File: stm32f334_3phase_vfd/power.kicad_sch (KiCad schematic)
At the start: 49 parts, among them J201 Conn_02x01, J202 Conn_02x01, J205 Conn_02x01, J206 TP_VBU, J207 TP_VBV, J208 TP_VBW, J209 Conn_02x01, J212 Conn_02x01, J213 TP_TSO, J214 Conn_02x01, J215 Conn_02x01, J218 TP_CSENSE, U201 STGIB15CH60TS-L

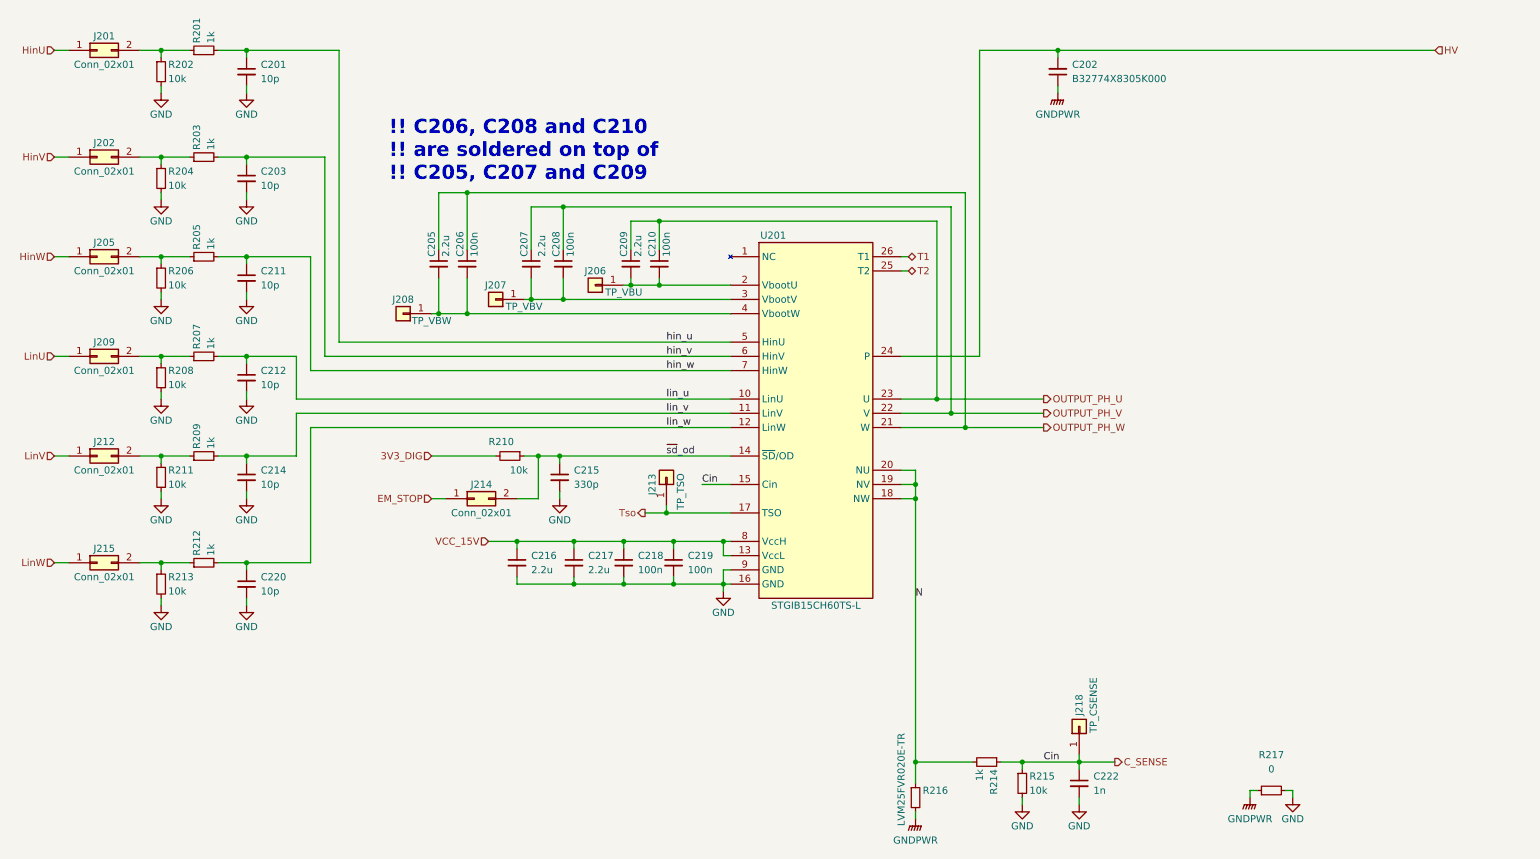
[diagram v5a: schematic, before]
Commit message: pcb fix and schematic clean-up
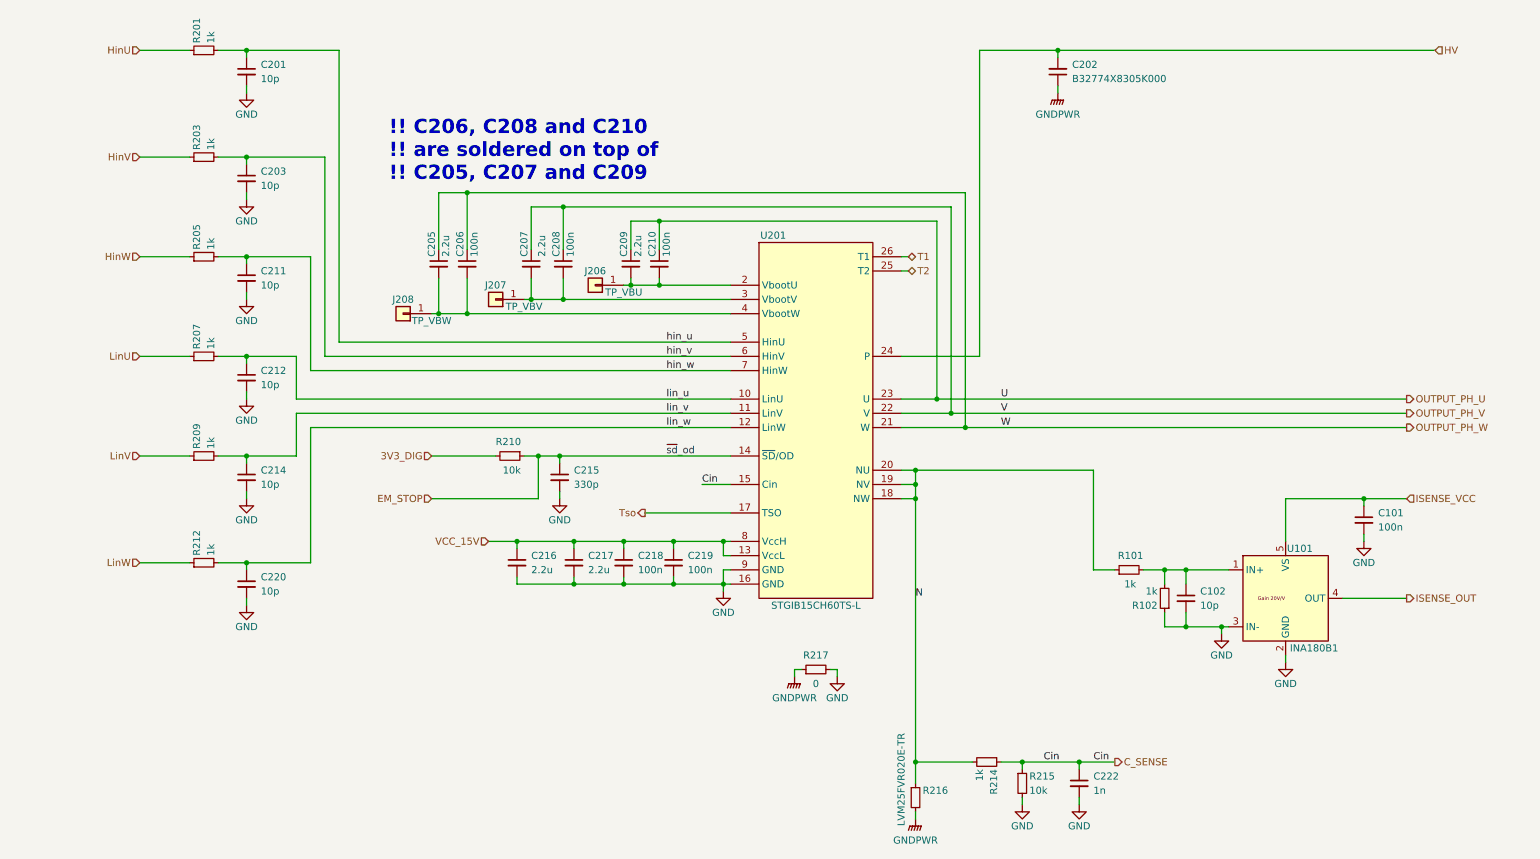
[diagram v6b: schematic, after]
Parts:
- removed J201, J202, J205, J209, J212, J214, J215: Conn_02x01, Connector_PinHeader_2.54mm:PinHeader_2x01_P2.54mm_Vertical, symbol Connector_Generic:Conn_02x01
- removed J213: TP_TSO, Connector_PinHeader_2.54mm:PinHeader_1x01_P2.54mm_Vertical, symbol Connector_Generic:Conn_01x01
- removed J218: TP_CSENSE, Connector_PinHeader_2.54mm:PinHeader_1x01_P2.54mm_Vertical, symbol Connector_Generic:Conn_01x01
- removed R202, R204, R206, R208, R211, R213: 10k, Resistor_SMD:R_1206_3216Metric, symbol Device:R_Small
- added C101: 100n, Capacitor_SMD:C_0805_2012Metric, symbol Device:C_Small
- added C102: 10p, Capacitor_SMD:C_0805_2012Metric, symbol Device:C_Small
- added R101, R102: 1k, Resistor_SMD:R_0805_2012Metric, symbol Device:R_Small
- added U101: INA180B1, Package_TO_SOT_SMD:SOT-23-5, symbol custom_parts:INA180B1
- C201, C203, C211, C212, C214, C215, C218, C219, C220, C222: footprint Capacitor_SMD:C_1206_3216Metric -> Capacitor_SMD:C_0805_2012Metric
- R201, R203, R205, R207, R209, R210, R212, R214, R215: footprint Resistor_SMD:R_1206_3216Metric -> Resistor_SMD:R_0805_2012Metric
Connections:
- net ~{sd}_od is gone; now on net EM_STOP: C215.1, R210.1, U201.14 (~{SD}/OD)
- net GND: now also C101.2, C102.2, R102.1, U101.2 (GND), U101.3 (IN-)
- net HinU: now also R201.1
- net HinV: now also R203.1
- net HinW: now also R205.1
- net LinU: now also R207.1
- net LinV: now also R209.1
- net LinW: now also R212.1
- net N: now also R101.1
- new net: C102.1, R101.2, R102.2, U101.1 (IN+)
- new net ISENSE_OUT: U101.4 (OUT)
- new net ISENSE_VCC: C101.1, U101.5 (VS)
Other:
- moved on the sheet: R217

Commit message: update schematic
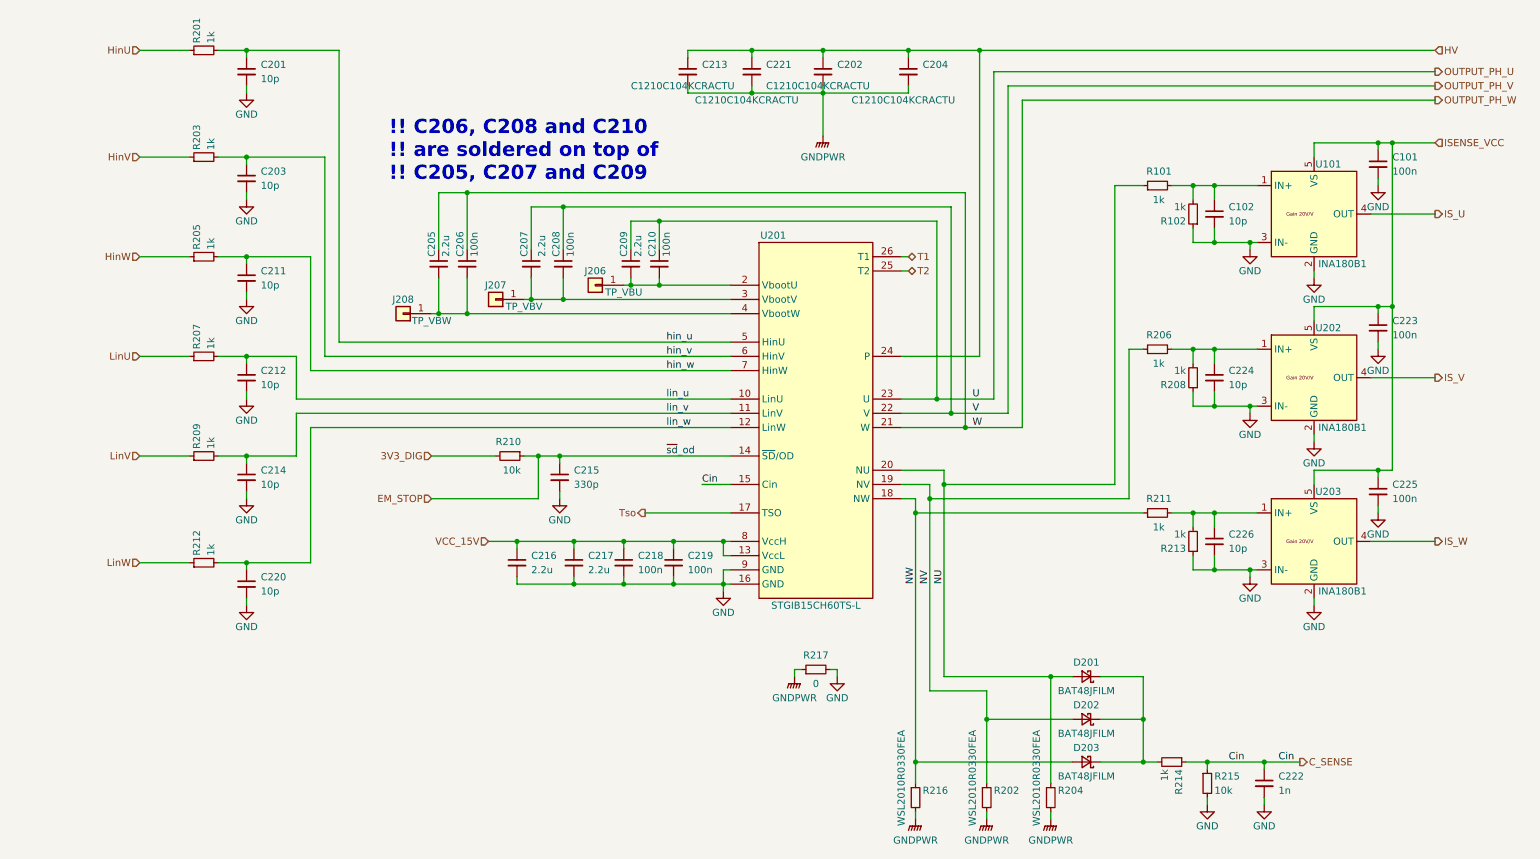
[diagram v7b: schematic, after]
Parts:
- added C204, C213, C221: C1210C104KCRACTU, Capacitor_SMD:C_1210_3225Metric, symbol Device:C_Small
- added C223, C225: 100n, Capacitor_SMD:C_0805_2012Metric, symbol Device:C_Small
- added C224, C226: 10p, Capacitor_SMD:C_0805_2012Metric, symbol Device:C_Small
- added D201, D202, D203: BAT48JFILM, Diode_SMD:D_SOD-323, symbol Device:D_Schottky_Small
- added R202, R204: WSL2010R0330FEA, Resistor_SMD:R_2010_5025Metric, symbol Device:R_Small
- added R206, R208, R211, R213: 1k, Resistor_SMD:R_0805_2012Metric, symbol Device:R_Small
- added U202, U203: INA180B1, Package_TO_SOT_SMD:SOT-23-5, symbol custom_parts:INA180B1
- C202: value B32774X8305K000 -> C1210C104KCRACTU; footprint Capacitor_THT:C_Rect_L31.5mm_W11.0mm_P27.50mm_MKS4 -> Capacitor_SMD:C_1210_3225Metric
- R216: value LVM25FVR020E-TR -> WSL2010R0330FEA; footprint Resistor_SMD:R_2512_6332Metric_Pad1.40x3.35mm_HandSolder -> Resistor_SMD:R_2010_5025Metric
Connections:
- net GND: now also C223.2, C224.2, C225.2, C226.2, R208.1, R213.1, U202.2 (GND), U202.3 (IN-), U203.2 (GND), U203.3 (IN-)
- net GNDPWR: now also C202.2, C204.2, C213.2, C221.2, R202.2, R204.2; no longer C202.1
- net HV: now also C202.1, C204.1, C213.1, C221.1; no longer C202.2
- net ISENSE_VCC: now also C223.1, C225.1, U202.5 (VS), U203.5 (VS)
- net ISENSE_OUT renamed IS_U
- removed net N: R101.1, R214.2, R216.1, U201.18 (NW), U201.19 (NV), U201.20 (NU)
- new net: C226.1, R211.2, R213.2, U203.1 (IN+)
- new net: D201.1 (K), D202.1 (K), D203.1 (K), R214.2
- new net: C224.1, R206.2, R208.2, U202.1 (IN+)
- new net IS_V: U202.4 (OUT)
- new net IS_W: U203.4 (OUT)
- new net NU: D201.2 (A), R101.1, R204.1, U201.20 (NU)
- new net NV: D202.2 (A), R202.1, R206.1, U201.19 (NV)
- new net NW: D203.2 (A), R211.1, R216.1, U201.18 (NW)
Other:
- moved on the sheet: C101, C102, C222, R101, R102, R214, R215, U101

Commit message: small updates in the schematic
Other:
- note added: "NOTE: 3V3_DIG can be powered from a GPIO input with pull-up, with R210 shorted That way enabling the pull-up takes the chip out of shutdown, and an falling edge IRQ can be used to detect overcurrent"
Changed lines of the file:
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@@
     (stroke (width 0) (type default) (color 0 0 0 0))
+  )
+  (text "NOTE: 3V3_DIG can be powered from a \nGPIO input with pull-up, with R210 shorted\nThat way enabling the pull-up takes the chip\nout of shutdown, and an falling edge IRQ\ncan be used to detect overcurrent"
+    (at 67.31 137.16 0)
+    (effects (font (size 1.27 1.27)) (justify left bottom))
   )
   (text "!! C206, C208 and C210\n!! are soldered on top of\n!! C205, C207 and C209"
